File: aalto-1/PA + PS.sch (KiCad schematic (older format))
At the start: 9 parts

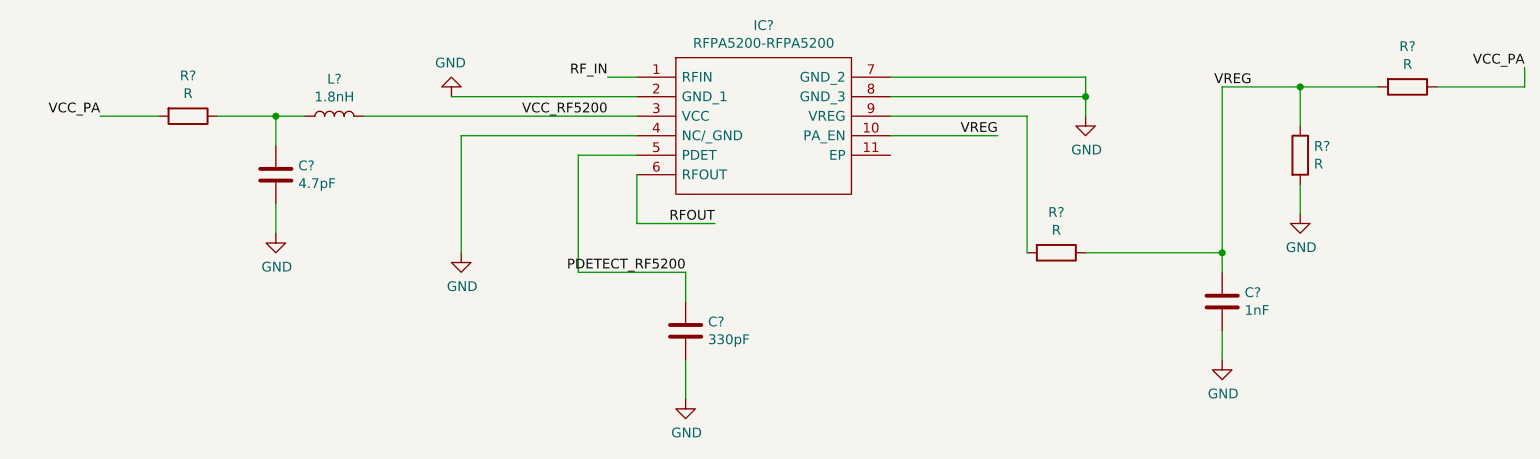
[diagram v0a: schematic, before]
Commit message: Edited PA to Larson's Suggestions
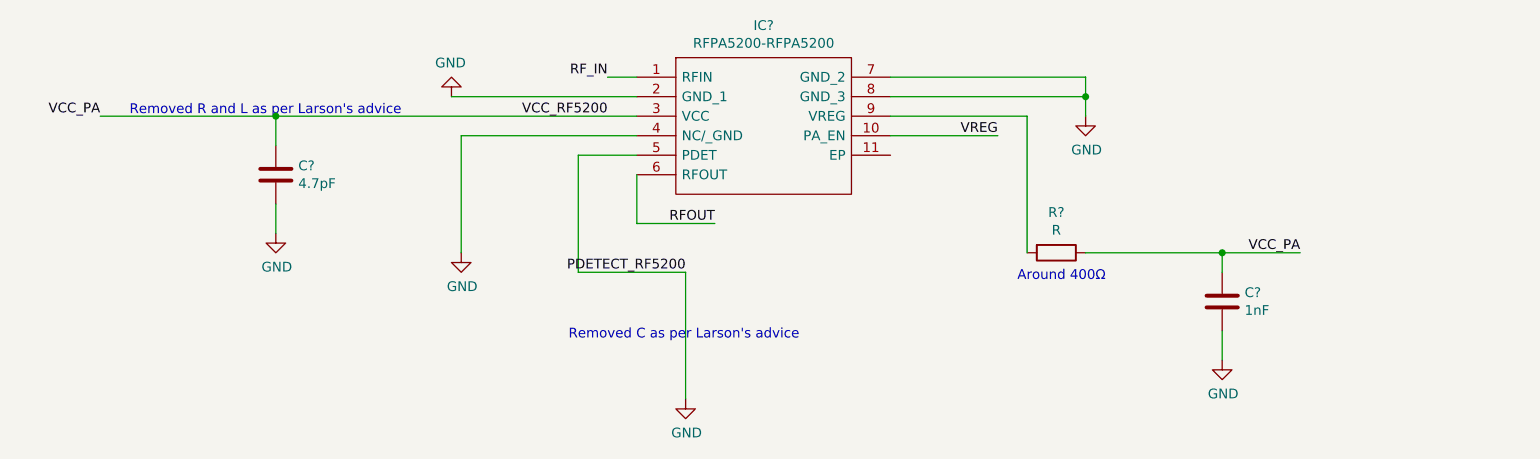
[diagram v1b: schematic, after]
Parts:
- removed C?: 330pF, symbol Device:C
- removed L?: 1.8nH, symbol Device:L
- removed R? (x3): R, symbol Device:R
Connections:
- net PDETECT_RF5200 is gone; now on net GND: IC?.5 (PDET)
- net VCC_RF5200 is gone; now on net VCC_PA: IC?.3 (VCC)
- net VCC_PA: now also C?.1, C?.1, R?.1
- net VREG: no longer C?.1, R?.1
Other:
- note added: "Around 400Ω\n"
- note added: "Removed C as per Larson's advice\n"
- note added: "Removed R and L as per Larson's advice\n"
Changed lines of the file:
@@
-$EndComp
-$Comp
-L Device:C C?
-U 1 1 60586D7C
-P 5500 5850
-F 0 "C?" H 5615 5896 50  0000 L CNN
-F 1 "330pF" H 5615 5805 50  0000 L CNN
-F 2 "" H 5538 5700 50  0001 C CNN
-F 3 "~" H 5500 5850 50  0001 C CNN
-	1    5500 5850
-	1    0    0    -1
 $EndComp
 $Comp
@@
 $EndComp
 Wire Wire Line
-	5500 6000 5500 6200
-Wire Wire Line
 	5500 5550 4950 5550
 Wire Wire Line
@@
 Wire Wire Line
 	4950 4950 5250 4950
-Wire Wire Line
-	5500 5550 5500 5700
 Text Label 5500 5550 2    50   ~ 0
 PDETECT_RF5200
@@
 $EndComp
 $Comp
-L Device:R R?
-U 1 1 6058DDFE
-P 8650 4950
-F 0 "R?" H 8720 4996 50  0000 L CNN
-F 1 "R" H 8720 4905 50  0000 L CNN
-F 2 "" V 8580 4950 50  0001 C CNN
-F 3 "~" H 8650 4950 50  0001 C CNN
-	1    8650 4950
-	1    0    0    -1
-$EndComp
-$Comp
-L Device:R R?
-U 1 1 6058E688
-P 9200 4600
-F 0 "R?" V 8993 4600 50  0000 C CNN
-F 1 "R" V 9084 4600 50  0000 C CNN
-F 2 "" V 9130 4600 50  0001 C CNN
-F 3 "~" H 9200 4600 50  0001 C CNN
-	1    9200 4600
-	0    1    1    0
-$EndComp
-$Comp
 L Device:C C?
 U 1 1 6058F151
@@
 Wire Wire Line
 	7550 5450 8250 5450
-Wire Wire Line
-	8250 5450 8250 4600
-Wire Wire Line
-	8250 4600 8650 4600
-Connection ~ 8250 5450
-Wire Wire Line
-	8650 4800 8650 4600
-Connection ~ 8650 4600
-Wire Wire Line
-	8650 4600 9050 4600
-$Comp
-L power:GND #PWR?
-U 1 1 60592C66
-P 8650 5250
-F 0 "#PWR?" H 8650 5000 50  0001 C CNN
-F 1 "GND" H 8655 5077 50  0000 C CNN
-F 2 "" H 8650 5250 50  0001 C CNN
-F 3 "" H 8650 5250 50  0001 C CNN
-	1    8650 5250
-	1    0    0    -1
-$EndComp
-Wire Wire Line
-	8650 5100 8650 5250
-Text Label 9800 4500 2    50   ~ 0
+Text Label 8650 5450 2    50   ~ 0
 VCC_PA
-Text Label 8400 4600 2    50   ~ 0
-VREG
-Wire Wire Line
-	9350 4600 9800 4600
-Wire Wire Line
-	9800 4600 9800 4500
-$Comp
-L Device:L L?
-U 1 1 605951BD
-P 3700 4750
-F 0 "L?" V 3890 4750 50  0000 C CNN
-F 1 "1.8nH" V 3799 4750 50  0000 C CNN
-F 2 "" H 3700 4750 50  0001 C CNN
-F 3 "~" H 3700 4750 50  0001 C CNN
-	1    3700 4750
-	0    -1   -1   0
-$EndComp
 $Comp
 L Device:C C?
@@
 	1    0    0    -1
 $EndComp
-$Comp
-L Device:R R?
-U 1 1 6059635B
-P 2950 4750
-F 0 "R?" V 2743 4750 50  0000 C CNN
-F 1 "R" V 2834 4750 50  0000 C CNN
-F 2 "" V 2880 4750 50  0001 C CNN
-F 3 "~" H 2950 4750 50  0001 C CNN
-	1    2950 4750
-	0    1    1    0
-$EndComp
-Wire Wire Line
-	3100 4750 3400 4750
-Wire Wire Line
-	3850 4750 5250 4750
 Wire Wire Line
 	3400 4900 3400 4750
 Connection ~ 3400 4750
-Wire Wire Line
-	3400 4750 3550 4750
 Text Label 2500 4750 2    50   ~ 0
 VCC_PA
-Wire Wire Line
-	2500 4750 2800 4750
 $Comp
 L power:GND #PWR?
@@
 Text Label 5100 4750 2    50   ~ 0
 VCC_RF5200
+Wire Wire Line
+	8250 5450 8650 5450
+Connection ~ 8250 5450
+Text Notes 7200 5600 0    50   ~ 0
+Around 400Ω\n
+Wire Wire Line
+	5500 5550 5500 6200
+Text Notes 4900 5900 0    50   ~ 0
+Removed C as per Larson's advice\n
+Wire Wire Line
+	2500 4750 3400 4750
+Wire Wire Line
+	3400 4750 5250 4750
+Text Notes 2650 4750 0    50   ~ 0
+Removed R and L as per Larson's advice\n
 $EndSCHEMATC

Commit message: Labeling schematics
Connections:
- net VREG: now also IC?.9 (VREG), R?.2
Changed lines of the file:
@@
 Wire Wire Line
 	4950 4950 5250 4950
-Text Label 5500 5550 2    50   ~ 0
-PDETECT_RF5200
 $Comp
 L power:GND #PWR?
@@
 Text Label 7100 4850 2    50   ~ 0
 VREG
-Wire Wire Line
-	6550 4850 7100 4850
 Text Label 5100 4550 2    50   ~ 0
 RF_IN
@@
 	6550 4750 7250 4750
 Wire Wire Line
-	7250 4750 7250 5450
+	7250 4750 7250 4850
 Wire Wire Line
 	8250 5450 8250 5550
-Wire Wire Line
-	7550 5450 8250 5450
-Text Label 8650 5450 2    50   ~ 0
-VCC_PA
 $Comp
 L Device:C C?
@@
 	3400 4900 3400 4750
 Connection ~ 3400 4750
-Text Label 2500 4750 2    50   ~ 0
-VCC_PA
 $Comp
 L power:GND #PWR?
@@
 Text Notes 2650 4750 0    50   ~ 0
 Removed R and L as per Larson's advice\n
+Text GLabel 8650 5450 2    50   Input ~ 0
+VCC_PA
+Text GLabel 2500 4750 0    50   Input ~ 0
+VCC_PA
+Text GLabel 5500 5550 2    50   Input ~ 0
+PDETECT_RF5200
+Wire Wire Line
+	7550 5450 8250 5450
+Wire Wire Line
+	6550 4850 7250 4850
+Connection ~ 7250 4850
+Wire Wire Line
+	7250 4850 7250 5450
 $EndSCHEMATC

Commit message: starting pcb layout
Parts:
- R3: renamed from R?; value R -> 400Ω
- gave numbers to parts that had none: 3
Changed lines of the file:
@@
 $EndDescr
 $Comp
-L aalto-1-rescue:RFPA5200-RFPA5200 IC?
+L aalto-1-rescue:RFPA5200-RFPA5200 IC3
 U 1 1 6057919A
 P 5250 4550
-F 0 "IC?" H 5900 4815 50  0000 C CNN
+F 0 "IC3" H 5900 4815 50  0000 C CNN
 F 1 "RFPA5200-RFPA5200" H 5900 4724 50  0000 C CNN
 F 2 "RFPA5200" H 6400 4650 50  0001 L CNN
@@
 $EndComp
 $Comp
-L power:GND #PWR?
+L power:GND #PWR016
 U 1 1 6058761D
 P 5500 6200
-F 0 "#PWR?" H 5500 5950 50  0001 C CNN
+F 0 "#PWR016" H 5500 5950 50  0001 C CNN
 F 1 "GND" H 5505 6027 50  0000 C CNN
 F 2 "" H 5500 6200 50  0001 C CNN
@@
 	4950 4950 5250 4950
 $Comp
-L power:GND #PWR?
+L power:GND #PWR015
 U 1 1 60588B39
 P 4350 5450
-F 0 "#PWR?" H 4350 5200 50  0001 C CNN
+F 0 "#PWR015" H 4350 5200 50  0001 C CNN
 F 1 "GND" H 4355 5277 50  0000 C CNN
 F 2 "" H 4350 5450 50  0001 C CNN
@@
 	5100 4550 5250 4550
 $Comp
-L power:GND #PWR?
+L power:GND #PWR014
 U 1 1 6058AB5F
 P 4300 4650
-F 0 "#PWR?" H 4300 4400 50  0001 C CNN
+F 0 "#PWR014" H 4300 4400 50  0001 C CNN
 F 1 "GND" H 4305 4477 50  0000 C CNN
 F 2 "" H 4300 4650 50  0001 C CNN
@@
 	5250 5300 5250 5050
 $Comp
-L power:GND #PWR?
+L power:GND #PWR017
 U 1 1 6058C322
 P 7550 4750
-F 0 "#PWR?" H 7550 4500 50  0001 C CNN
+F 0 "#PWR017" H 7550 4500 50  0001 C CNN
 F 1 "GND" H 7555 4577 50  0000 C CNN
 F 2 "" H 7550 4750 50  0001 C CNN
@@
 	7550 4650 7550 4750
 $Comp
-L Device:R R?
+L Device:R R3
 U 1 1 6058D759
 P 7400 5450
-F 0 "R?" V 7193 5450 50  0000 C CNN
-F 1 "R" V 7284 5450 50  0000 C CNN
+F 0 "R3" V 7193 5450 50  0000 C CNN
+F 1 "400Ω" V 7284 5450 50  0000 C CNN
 F 2 "" V 7330 5450 50  0001 C CNN
 F 3 "~" H 7400 5450 50  0001 C CNN
@@
 $EndComp
 $Comp
-L Device:C C?
+L Device:C C7
 U 1 1 6058F151
 P 8250 5700
-F 0 "C?" H 8365 5746 50  0000 L CNN
+F 0 "C7" H 8365 5746 50  0000 L CNN
 F 1 "1nF" H 8365 5655 50  0000 L CNN
 F 2 "" H 8288 5550 50  0001 C CNN
@@
 $EndComp
 $Comp
-L power:GND #PWR?
+L power:GND #PWR018
 U 1 1 6058FB72
 P 8250 6000
-F 0 "#PWR?" H 8250 5750 50  0001 C CNN
+F 0 "#PWR018" H 8250 5750 50  0001 C CNN
 F 1 "GND" H 8255 5827 50  0000 C CNN
 F 2 "" H 8250 6000 50  0001 C CNN
@@
 	8250 5450 8250 5550
 $Comp
-L Device:C C?
+L Device:C C6
 U 1 1 60595AE6
 P 3400 5050
-F 0 "C?" H 3515 5096 50  0000 L CNN
+F 0 "C6" H 3515 5096 50  0000 L CNN
 F 1 "4.7pF" H 3515 5005 50  0000 L CNN
 F 2 "" H 3438 4900 50  0001 C CNN
@@
 Connection ~ 3400 4750
 $Comp
-L power:GND #PWR?
+L power:GND #PWR013
 U 1 1 60598A3A
 P 3400 5350
-F 0 "#PWR?" H 3400 5100 50  0001 C CNN
+F 0 "#PWR013" H 3400 5100 50  0001 C CNN
 F 1 "GND" H 3405 5177 50  0000 C CNN
 F 2 "" H 3400 5350 50  0001 C CNN

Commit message: footprint libraries
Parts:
- IC3: footprint RFPA5200 -> RFPA5200:RFPA5200
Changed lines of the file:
@@
 F 0 "IC3" H 5900 4815 50  0000 C CNN
 F 1 "RFPA5200-RFPA5200" H 5900 4724 50  0000 C CNN
-F 2 "RFPA5200" H 6400 4650 50  0001 L CNN
+F 2 "RFPA5200:RFPA5200" H 6400 4650 50  0001 L CNN
 F 3 "https://www.qorvo.com/products/d/da001012" H 6400 4550 50  0001 L CNN
 F 4 "RF Amplifier 2.4-2.5GHz Gain 33dB Pout 27dBm 5V" H 6400 4450 50  0001 L CNN "Description"
@@
 $EndComp
 $Comp
-L power:GND #PWR016
+L aalto-1-rescue:GND-power #PWR016
 U 1 1 6058761D
 P 5500 6200
@@
 	4950 4950 5250 4950
 $Comp
-L power:GND #PWR015
+L aalto-1-rescue:GND-power #PWR015
 U 1 1 60588B39
 P 4350 5450
@@
 	5100 4550 5250 4550
 $Comp
-L power:GND #PWR014
+L aalto-1-rescue:GND-power #PWR014
 U 1 1 6058AB5F
 P 4300 4650
@@
 	5250 5300 5250 5050
 $Comp
-L power:GND #PWR017
+L aalto-1-rescue:GND-power #PWR017
 U 1 1 6058C322
 P 7550 4750
@@
 $EndComp
 $Comp
-L power:GND #PWR018
+L aalto-1-rescue:GND-power #PWR018
 U 1 1 6058FB72
 P 8250 6000
@@
 Connection ~ 3400 4750
 $Comp
-L power:GND #PWR013
+L aalto-1-rescue:GND-power #PWR013
 U 1 1 60598A3A
 P 3400 5350

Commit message: Fall 2021
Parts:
- C6, C7: footprint (none) -> Capacitor_SMD:C_0805_2012Metric
- R3: footprint (none) -> Resistor_SMD:R_0805_2012Metric
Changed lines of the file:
@@
 F 0 "R3" V 7193 5450 50  0000 C CNN
 F 1 "400Ω" V 7284 5450 50  0000 C CNN
-F 2 "" V 7330 5450 50  0001 C CNN
+F 2 "Resistor_SMD:R_0805_2012Metric" V 7330 5450 50  0001 C CNN
 F 3 "~" H 7400 5450 50  0001 C CNN
 	1    7400 5450
@@
 F 0 "C7" H 8365 5746 50  0000 L CNN
 F 1 "1nF" H 8365 5655 50  0000 L CNN
-F 2 "" H 8288 5550 50  0001 C CNN
+F 2 "Capacitor_SMD:C_0805_2012Metric" H 8288 5550 50  0001 C CNN
 F 3 "~" H 8250 5700 50  0001 C CNN
 	1    8250 5700
@@
 F 0 "C6" H 3515 5096 50  0000 L CNN
 F 1 "4.7pF" H 3515 5005 50  0000 L CNN
-F 2 "" H 3438 4900 50  0001 C CNN
+F 2 "Capacitor_SMD:C_0805_2012Metric" H 3438 4900 50  0001 C CNN
 F 3 "~" H 3400 5050 50  0001 C CNN
 	1    3400 5050
